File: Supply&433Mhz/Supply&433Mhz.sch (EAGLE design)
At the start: 17 parts, among them K1 61004021821, P1 DF11-06-2DS, Q1 BS170

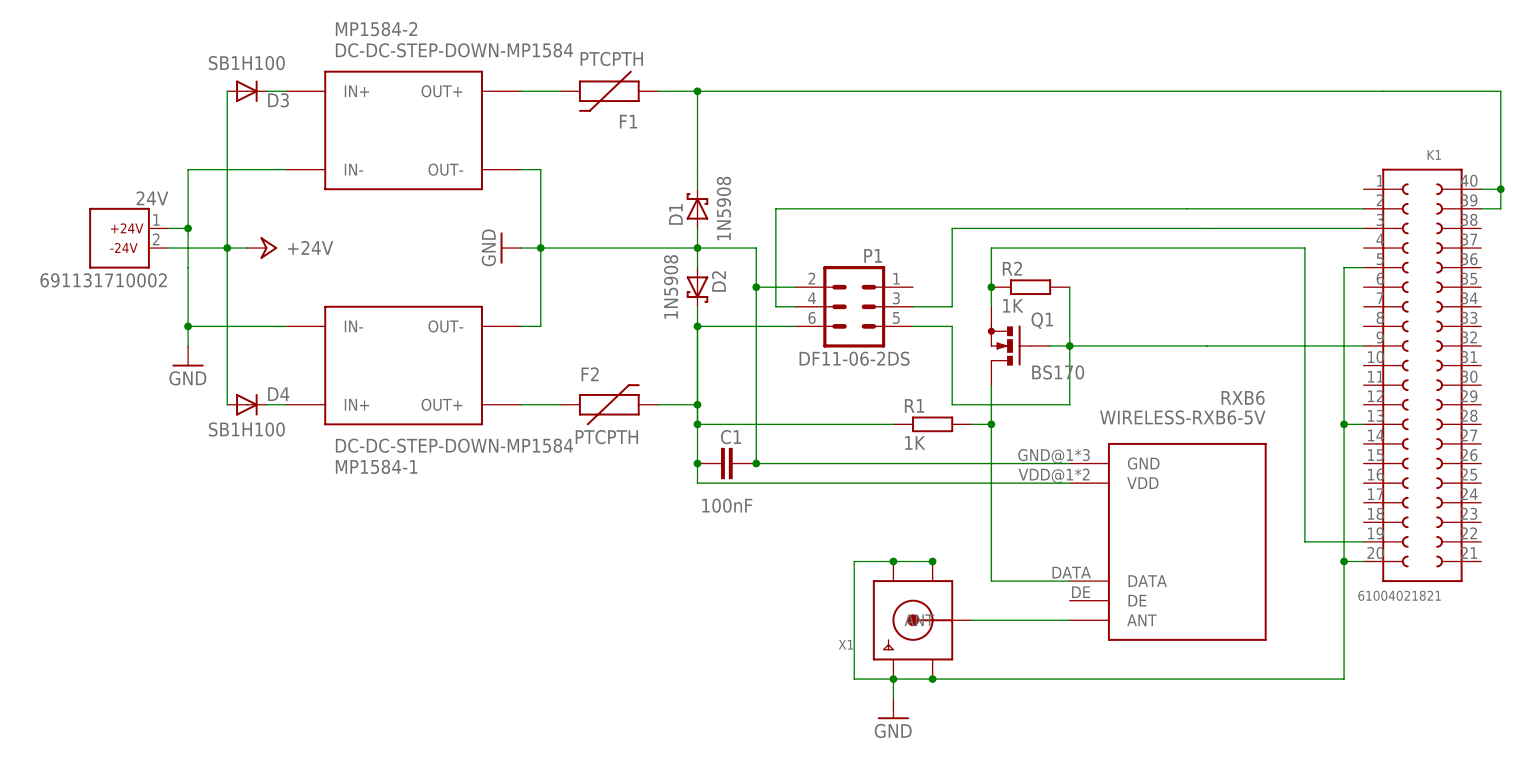
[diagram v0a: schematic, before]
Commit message: Remove pull-up to 5V since level-shifter worked not properly. Use 10K instead of 1K resistor as pull-up to 3.3V.
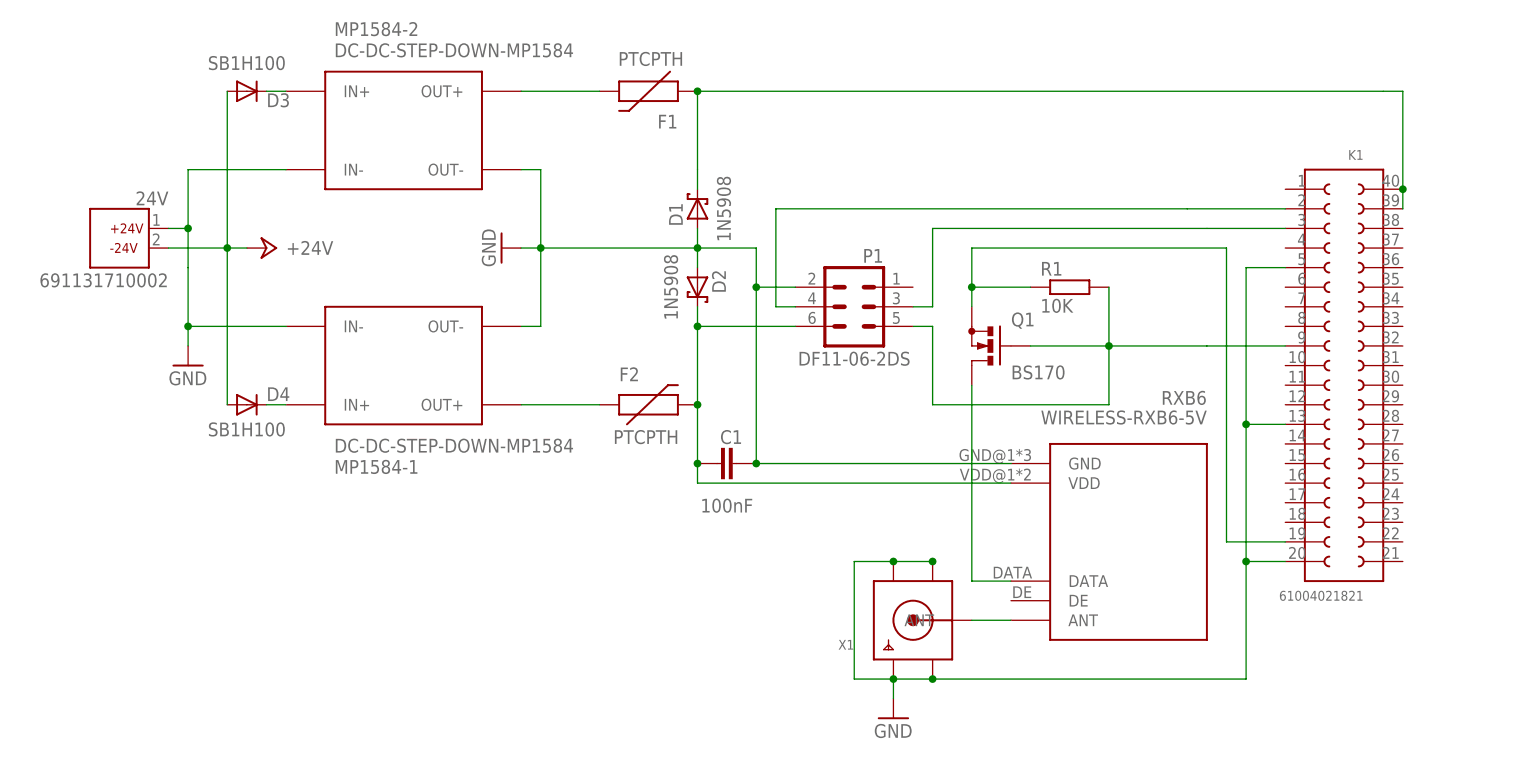
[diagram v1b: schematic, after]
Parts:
- removed R2: 1K, rcl:R-EU_0204/2V
- R1: value 1K -> 10K
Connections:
- net N$11: now also R1.2; no longer R2.2
- net N$2: no longer R1.1
- net N$3: no longer R1.2
- net N$69: now also R1.1; no longer R2.1
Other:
- moved on the sheet: F1, F2, K1, Q1, R1, RXB6

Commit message: Use external 3.3V supply instead of raspberry one.
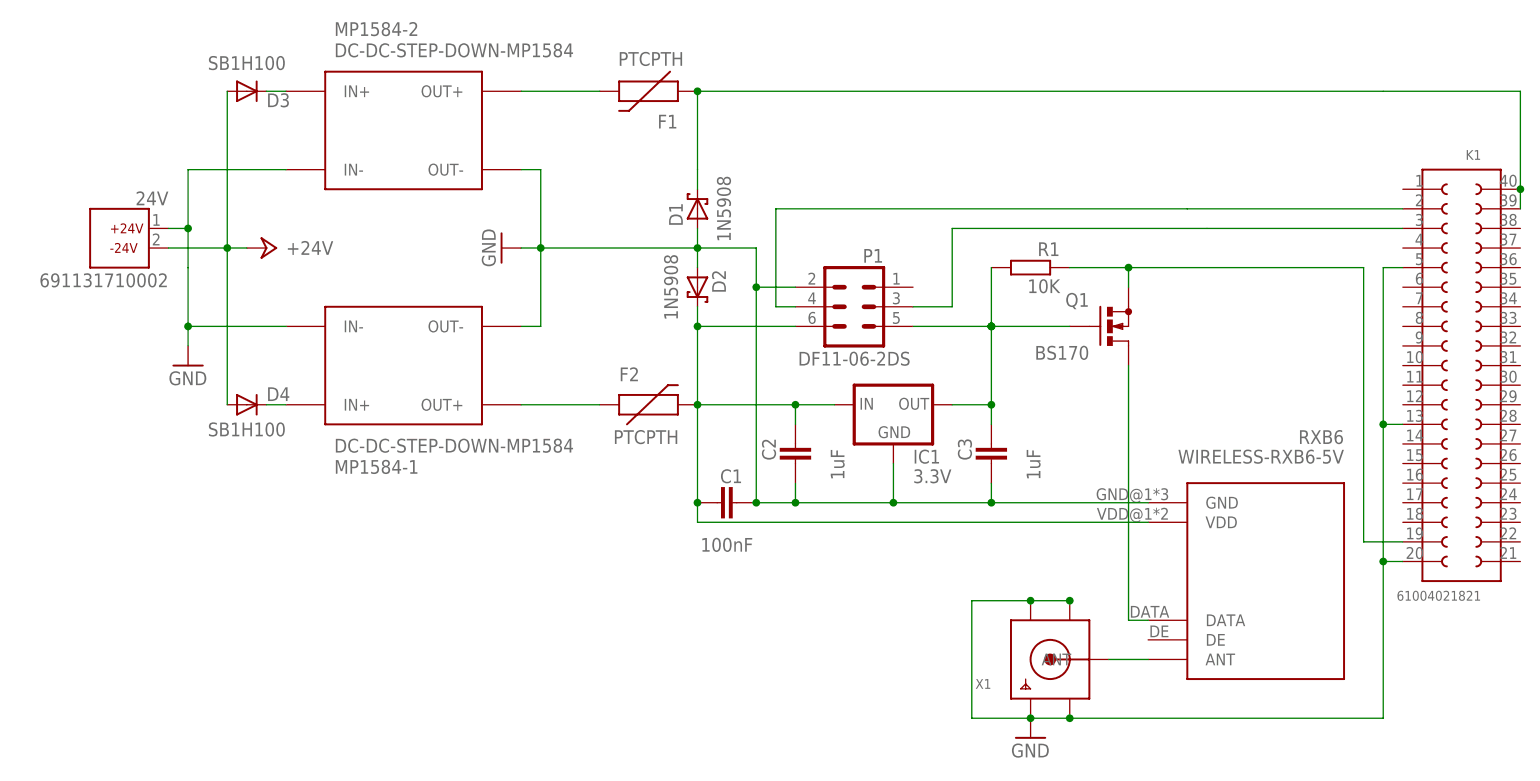
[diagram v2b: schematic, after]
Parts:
- added C2, C3: 1uF, capacitor-wima:C5/3
- added IC1: 3.3V, adafruit:MCP1700INLINE
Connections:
- net GND: now also C2.2, C3.2, IC1.GND
- net N$11: now also C3.1, IC1.OUT; no longer K1.9
- net N$2: now also C2.1, IC1.IN
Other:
- moved on the sheet: C1, K1, Q1, R1, RXB6, X1
